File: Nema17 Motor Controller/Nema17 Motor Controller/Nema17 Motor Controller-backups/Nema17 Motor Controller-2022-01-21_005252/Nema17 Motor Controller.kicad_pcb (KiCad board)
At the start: 4 copper layers, 42.1 x 42.1 mm, 42 parts, among them J1 Power In, J2 ARM-JTAG/SWD_10, J3 Motor Out, J4 Serial Out, SW1 Reset, U1 STM32L011F4Px, U2 R-78B5.0-2.0, U3 AMS1117-3.3, U4 AS5047D

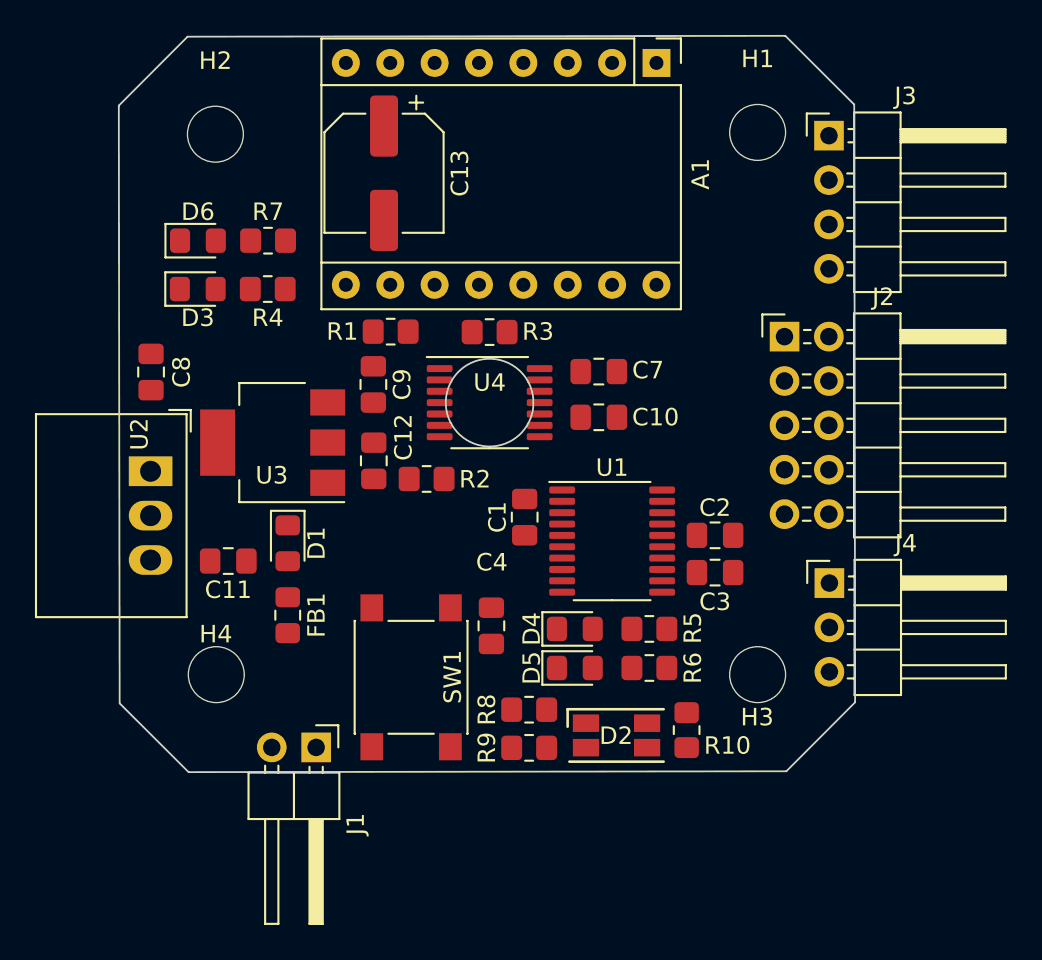
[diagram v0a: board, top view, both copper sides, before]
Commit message: update
pcb design continued, Motor control for position velocity and acceleration
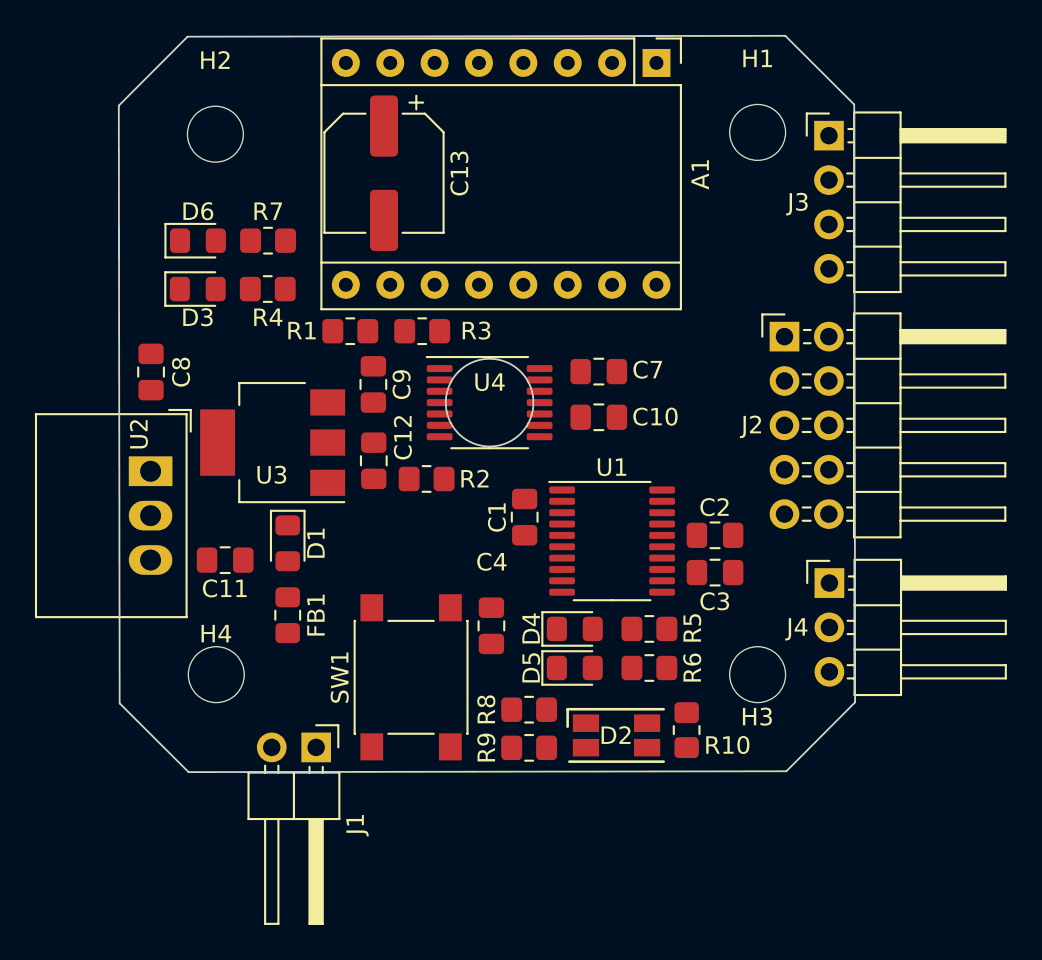
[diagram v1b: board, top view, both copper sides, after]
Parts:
- SW1: footprint Button_Switch_SMD:SW_Push_1P1T_NO_6x6mm_H9.5mm -> Button_Switch_SMD:SW_SPST_PTS645
- moved R3 3.86 mm to (143.5, 97.4), turned to 0 degrees
- moved R1 2.31 mm to (139.4, 97.4)
- moved C11 0.18 mm to (132.2, 110.5)
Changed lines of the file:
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@@
   (net 20 "Net-(D5-Pad2)")
   (net 21 "Net-(D6-Pad2)")
-  (net 22 "Net-(J1-Pad2)")
+  (net 22 "Net-(FB1-Pad1)")
   (net 23 "SWDIO")
   (net 24 "SWCLK")
@@
     (property "Sheetname" "")
     (attr through_hole)
-    (fp_text reference "J3" (at 4.385 -2.27) (layer "F.SilkS")
+    (fp_text reference "J3" (at -1.7464 3.8254) (layer "F.SilkS")
       (effects (font (size 1 1) (thickness 0.15)))
     )
@@
     )
   )
-  (footprint "Button_Switch_SMD:SW_Push_1P1T_NO_6x6mm_H9.5mm" (layer "F.Cu")
+  (footprint "Button_Switch_SMD:SW_SPST_PTS645" (layer "F.Cu")
     (at 142.875 117.2464 90)
-    (descr "tactile push button, 6x6mm e.g. PTS645xx series, height=9.5mm")
-    (tags "tact sw push 6mm smd")
-    (property "Sheetfile" "Nema17 Motor Controller.kicad_sch")
-    (property "Sheetname" "")
-    (attr smd)
-    (fp_text reference "SW1" (at 0.0254 2.3876 90) (layer "F.SilkS")
-      (effects (font (size 1 1) (thickness 0.15)))
-    )
-    (fp_text value "Reset" (at 0.0508 0.0762 90) (layer "F.Fab")
-      (effects (font (size 1 1) (thickness 0.15)))
-    )
-    (fp_text user "${REFERENCE}" (at 0 -2.286 90) (layer "F.Fab")
-      (effects (font (size 1 1) (thickness 0.15)))
-    )
+    (descr "C&K Components SPST SMD PTS645 Series 6mm Tact Switch")
+    (tags "SPST Button Switch")
+    (property "Sheetfile" "Nema17 Motor Controller.kicad_sch")
+    (property "Sheetname" "")
+    (attr smd)
+    (fp_text reference "SW1" (at 0 -4.05 90) (layer "F.SilkS")
+      (effects (font (size 1 1) (thickness 0.15)))
+    )
+    (fp_text value "Reset" (at 0 4.15 90) (layer "F.Fab")
+      (effects (font (size 1 1) (thickness 0.15)))
+    )
+    (fp_text user "${REFERENCE}" (at 0 -4.05 90) (layer "F.Fab")
+      (effects (font (size 1 1) (thickness 0.15)))
+    )
+    (fp_line (start 3.23 -3.23) (end 3.23 -3.2) (layer "F.SilkS") (width 0.12))
+    (fp_line (start -3.23 -3.2) (end -3.23 -3.23) (layer "F.SilkS") (width 0.12))
     (fp_line (start -3.23 3.23) (end -3.23 3.2) (layer "F.SilkS") (width 0.12))
+    (fp_line (start 3.23 -1.3) (end 3.23 1.3) (layer "F.SilkS") (width 0.12))
     (fp_line (start -3.23 -3.23) (end 3.23 -3.23) (layer "F.SilkS") (width 0.12))
+    (fp_line (start 3.23 3.23) (end 3.23 3.2) (layer "F.SilkS") (width 0.12))
+    (fp_line (start -3.23 3.23) (end 3.23 3.23) (layer "F.SilkS") (width 0.12))
     (fp_line (start -3.23 -1.3) (end -3.23 1.3) (layer "F.SilkS") (width 0.12))
-    (fp_line (start -3.23 3.23) (end 3.23 3.23) (layer "F.SilkS") (width 0.12))
-    (fp_line (start 3.23 -3.23) (end 3.23 -3.2) (layer "F.SilkS") (width 0.12))
-    (fp_line (start 3.23 -1.3) (end 3.23 1.3) (layer "F.SilkS") (width 0.12))
-    (fp_line (start 3.23 3.23) (end 3.23 3.2) (layer "F.SilkS") (width 0.12))
-    (fp_line (start -3.23 -3.2) (end -3.23 -3.23) (layer "F.SilkS") (width 0.12))
-    (fp_line (start -5 -3.25) (end -5 3.25) (layer "F.CrtYd") (width 0.05))
-    (fp_line (start -5 3.25) (end 5 3.25) (layer "F.CrtYd") (width 0.05))
-    (fp_line (start 5 3.25) (end 5 -3.25) (layer "F.CrtYd") (width 0.05))
-    (fp_line (start -5 -3.25) (end 5 -3.25) (layer "F.CrtYd") (width 0.05))
+    (fp_line (start -5.05 -3.4) (end -5.05 3.4) (layer "F.CrtYd") (width 0.05))
+    (fp_line (start -5.05 -3.4) (end 5.05 -3.4) (layer "F.CrtYd") (width 0.05))
+    (fp_line (start -5.05 3.4) (end 5.05 3.4) (layer "F.CrtYd") (width 0.05))
+    (fp_line (start 5.05 3.4) (end 5.05 -3.4) (layer "F.CrtYd") (width 0.05))
+    (fp_line (start -3 3) (end 3 3) (layer "F.Fab") (width 0.1))
+    (fp_line (start 3 3) (end 3 -3) (layer "F.Fab") (width 0.1))
     (fp_line (start 3 -3) (end -3 -3) (layer "F.Fab") (width 0.1))
     (fp_line (start -3 -3) (end -3 3) (layer "F.Fab") (width 0.1))
-    (fp_line (start -3 3) (end 3 3) (layer "F.Fab") (width 0.1))
-    (fp_line (start 3 3) (end 3 -3) (layer "F.Fab") (width 0.1))
     (fp_circle (center 0 0) (end 1.75 -0.05) (layer "F.Fab") (width 0.1) (fill none))
-    (pad "1" smd rect locked (at -3.975 -2.25 90) (size 1.55 1.3) (layers "F.Cu" "F.Paste" "F.Mask")
+    (pad "1" smd rect locked (at -3.98 -2.25 90) (size 1.55 1.3) (layers "F.Cu" "F.Paste" "F.Mask")
       (net 1 "GND") (pinfunction "1") (pintype "passive"))
-    (pad "1" smd rect locked (at 3.975 -2.25 90) (size 1.55 1.3) (layers "F.Cu" "F.Paste" "F.Mask")
+    (pad "1" smd rect locked (at 3.98 -2.25 90) (size 1.55 1.3) (layers "F.Cu" "F.Paste" "F.Mask")
       (net 1 "GND") (pinfunction "1") (pintype "passive"))
-    (pad "2" smd rect locked (at -3.975 2.25 90) (size 1.55 1.3) (layers "F.Cu" "F.Paste" "F.Mask")
+    (pad "2" smd rect locked (at 3.98 2.25 90) (size 1.55 1.3) (layers "F.Cu" "F.Paste" "F.Mask")
       (net 8 "Driver Reset") (pinfunction "2") (pintype "passive"))
-    (pad "2" smd rect locked (at 3.975 2.25 90) (size 1.55 1.3) (layers "F.Cu" "F.Paste" "F.Mask")
+    (pad "2" smd rect locked (at -3.98 2.25 90) (size 1.55 1.3) (layers "F.Cu" "F.Paste" "F.Mask")
       (net 8 "Driver Reset") (pinfunction "2") (pintype "passive"))
-    (model "${KICAD6_3DMODEL_DIR}/Button_Switch_SMD.3dshapes/SW_PUSH_6mm_H9.5mm.wrl"
+    (model "${KICAD6_3DMODEL_DIR}/Button_Switch_SMD.3dshapes/SW_SPST_PTS645.wrl"
       (offset (xyz 0 0 0))
       (scale (xyz 1 1 1))
@@
     (property "Sheetname" "")
     (attr through_hole)
-    (fp_text reference "J2" (at 5.655 -2.27) (layer "F.SilkS")
+    (fp_text reference "J2" (at -1.843 5.075) (layer "F.SilkS")
       (effects (font (size 1 1) (thickness 0.15)))
     )
@@
   )
   (footprint "Resistor_SMD:R_0805_2012Metric_Pad1.20x1.40mm_HandSolder" (layer "F.Cu")
-    (at 147.3708 97.4852 180)
+    (at 143.51 97.4344)
     (descr "Resistor SMD 0805 (2012 Metric), square (rectangular) end terminal, IPC_7351 nominal with elongated pad for handsoldering. (Body size source: IPC-SM-782 page 72, https://www.pcb-3d.com/wordpress/wp-content/uploads/ipc-sm-782a_amendment_1_and_2.pdf), generated with kicad-footprint-generator")
     (tags "resistor handsolder")
@@
     (property "Sheetname" "")
     (attr smd)
-    (fp_text reference "R3" (at -2.7686 0.0254) (layer "F.SilkS")
+    (fp_text reference "R3" (at 3.0988 0) (layer "F.SilkS")
       (effects (font (size 1 1) (thickness 0.15)))
     )
@@
     (fp_line (start -1 0.625) (end -1 -0.625) (layer "F.Fab") (width 0.1))
     (fp_line (start 1 0.625) (end -1 0.625) (layer "F.Fab") (width 0.1))
-    (pad "1" smd roundrect locked (at -1 0 180) (size 1.2 1.4) (layers "F.Cu" "F.Paste" "F.Mask") (roundrect_rratio 0.208333)
+    (pad "1" smd roundrect locked (at -1 0) (size 1.2 1.4) (layers "F.Cu" "F.Paste" "F.Mask") (roundrect_rratio 0.208333)
       (net 13 "+5V") (pintype "passive"))
-    (pad "2" smd roundrect locked (at 1 0 180) (size 1.2 1.4) (layers "F.Cu" "F.Paste" "F.Mask") (roundrect_rratio 0.208333)
+    (pad "2" smd roundrect locked (at 1 0) (size 1.2 1.4) (layers "F.Cu" "F.Paste" "F.Mask") (roundrect_rratio 0.208333)
       (net 45 "Net-(R3-Pad2)") (pintype "passive"))
     (model "${KICAD6_3DMODEL_DIR}/Resistor_SMD.3dshapes/R_0805_2012Metric.wrl"
@@
     (property "Sheetname" "")
     (attr through_hole)
-    (fp_text reference "J4" (at 4.385 -2.27) (layer "F.SilkS")
+    (fp_text reference "J4" (at -1.8226 2.5504) (layer "F.SilkS")
       (effects (font (size 1 1) (thickness 0.15)))
     )
@@
   )
   (footprint "Capacitor_SMD:C_0805_2012Metric_Pad1.18x1.45mm_HandSolder" (layer "F.Cu")
-    (at 132.4102 110.5916)
+    (at 132.2324 110.5408)
     (descr "Capacitor SMD 0805 (2012 Metric), square (rectangular) end terminal, IPC_7351 nominal with elongated pad for handsoldering. (Body size source: IPC-SM-782 page 76, https://www.pcb-3d.com/wordpress/wp-content/uploads/ipc-sm-782a_amendment_1_and_2.pdf, https://docs.google.com/spreadsheets/d/1BsfQQcO9C6DZCsRaXUlFlo91Tg2WpOkGARC1WS5S8t0/edit?usp=sharing), generated with kicad-footprint-generator")
     (tags "capacitor handsolder")
@@
     (fp_line (start -1 0.6) (end -1 -0.6) (layer "F.Fab") (width 0.1))
     (pad "1" smd roundrect locked (at -1.025 0 90) (size 1.15 1.4) (layers "F.Cu" "F.Paste" "F.Mask") (roundrect_rratio 0.217391)
-      (net 22 "Net-(J1-Pad2)") (pintype "passive"))
+      (net 22 "Net-(FB1-Pad1)") (pintype "passive"))
     (pad "2" smd roundrect locked (at 1.025 0 90) (size 1.15 1.4) (layers "F.Cu" "F.Paste" "F.Mask") (roundrect_rratio 0.217391)
       (net 14 "Net-(D1-Pad2)") (pintype "passive"))
@@
   )
   (footprint "Resistor_SMD:R_0805_2012Metric_Pad1.20x1.40mm_HandSolder" (layer "F.Cu")
-    (at 141.7066 97.4598)
+    (at 139.3952 97.4344)
     (descr "Resistor SMD 0805 (2012 Metric), square (rectangular) end terminal, IPC_7351 nominal with elongated pad for handsoldering. (Body size source: IPC-SM-782 page 72, https://www.pcb-3d.com/wordpress/wp-content/uploads/ipc-sm-782a_amendment_1_and_2.pdf), generated with kicad-footprint-generator")
     (tags "resistor handsolder")
@@
       (net 1 "GND") (pinfunction "Pin_1") (pintype "passive"))
     (pad "2" thru_hole oval locked (at 0 2.54 270) (size 1.7 1.7) (drill 1) (layers *.Cu *.Mask)
-      (net 22 "Net-(J1-Pad2)") (pinfunction "Pin_2") (pintype "passive"))
+      (net 22 "Net-(FB1-Pad1)") (pinfunction "Pin_2") (pintype "passive"))
     (model "${KICAD6_3DMODEL_DIR}/Connector_PinHeader_2.54mm.3dshapes/PinHeader_1x02_P2.54mm_Horizontal.wrl"
       (offset (xyz 0 0 0))
